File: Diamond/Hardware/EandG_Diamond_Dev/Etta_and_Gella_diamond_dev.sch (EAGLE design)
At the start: 122 parts, among them Q1 ZXMP6A13F, U1 ATSAMD21G-A, U2 3.3V, U5 OPA344, U6 ADMP401, U7 APDS-9960, Y1 32.768kHz

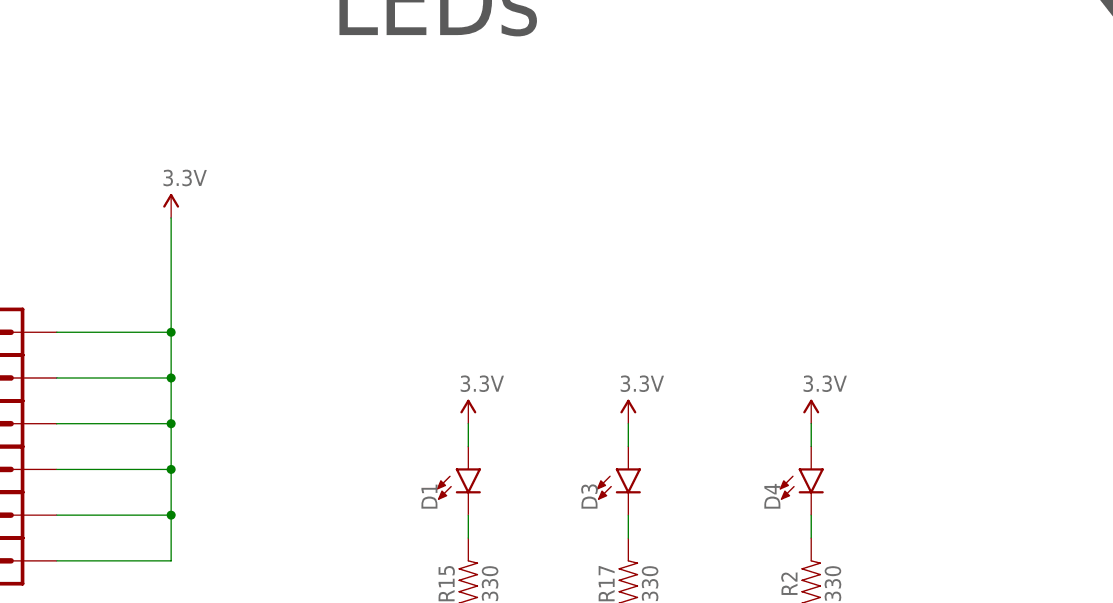
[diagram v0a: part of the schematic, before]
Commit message: Moved LEDs to D7, changed pinout on the right chevron, etc.
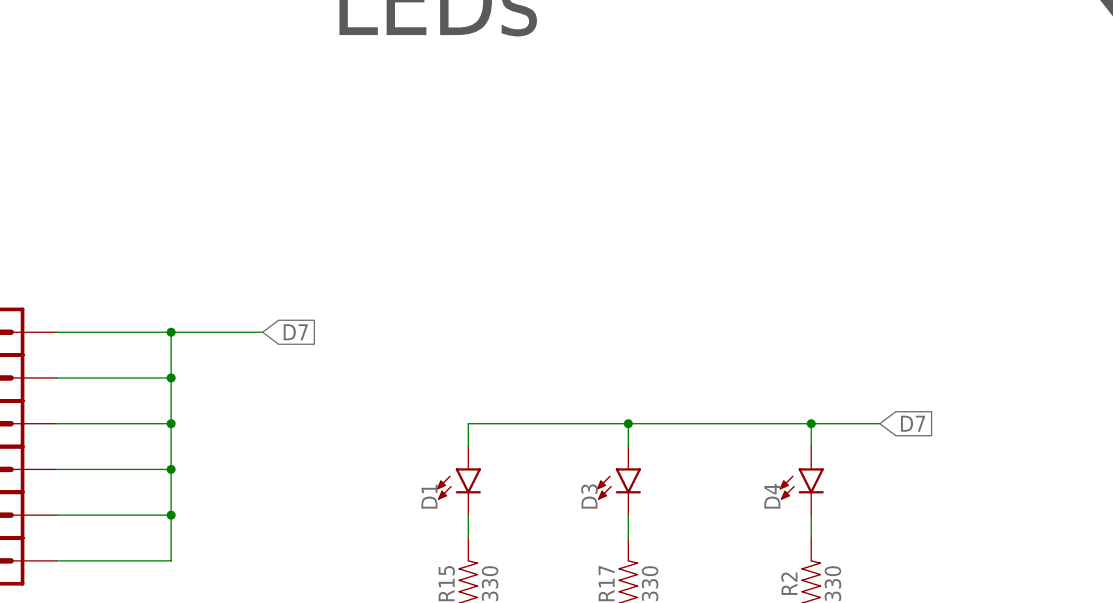
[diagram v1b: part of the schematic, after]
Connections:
- net 3.3V: no longer D1.A, D3.A, D4.A, J20.1, J62.1, J64.1, J68.1, J70.1, J77.1
- net D7: now also D1.A, D3.A, D4.A, J20.1, J62.1, J64.1, J68.1, J70.1, J77.1
